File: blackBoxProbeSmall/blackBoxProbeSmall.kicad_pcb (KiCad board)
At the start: 4 copper layers, 44 x 44 mm, 84 parts, among them J1 USB-ID, J2 JTAG_2X05, J3 JTAG_2X05, J4 Conn_01x04, Q1 Q_NMOS_DUAL, Q2 Q_PMOS_DUAL, U1 MCP1702-MB, U2 USBLC6-2, U3 STM32F103CBT, U4 74X2T45, U5 74X2T45, U6 74X2T45, U7 74X2T45, Y1 8.000MHz

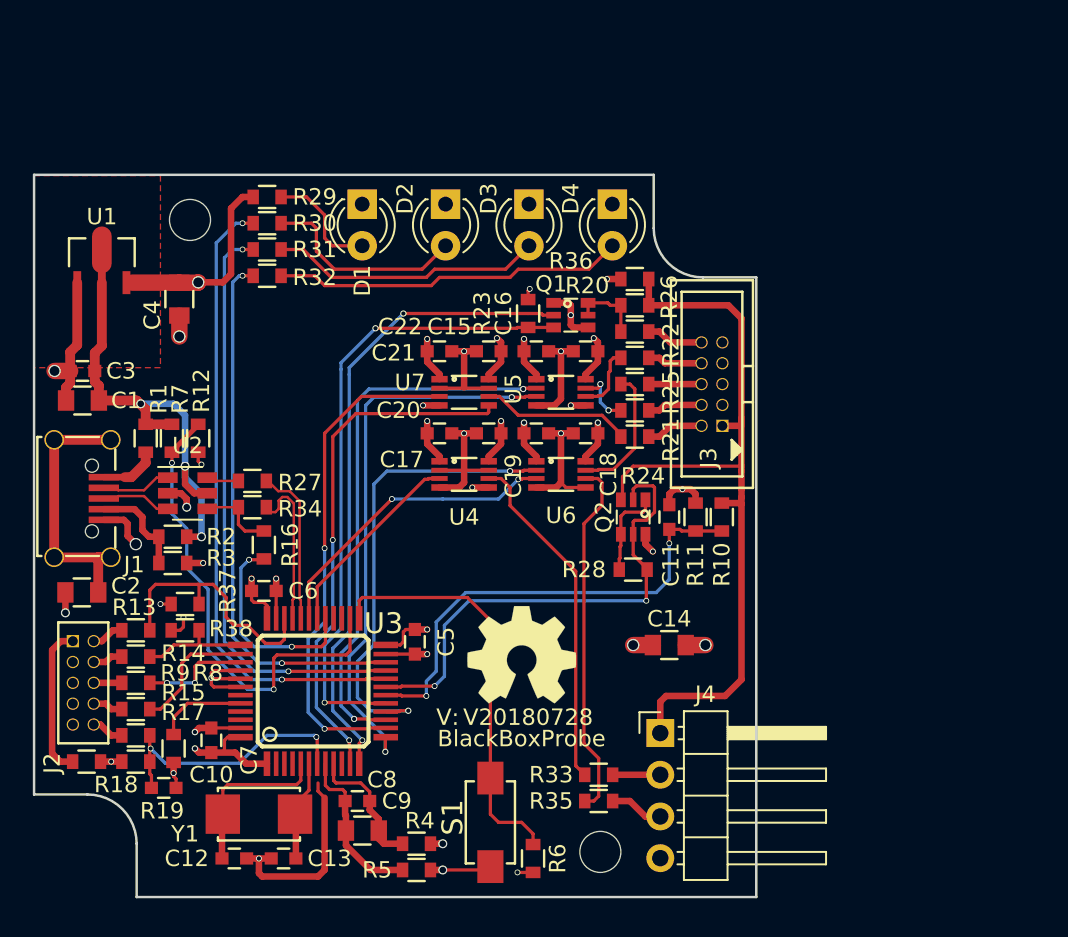
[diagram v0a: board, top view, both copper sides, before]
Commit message: replaced all R's C's and inserted new box outline
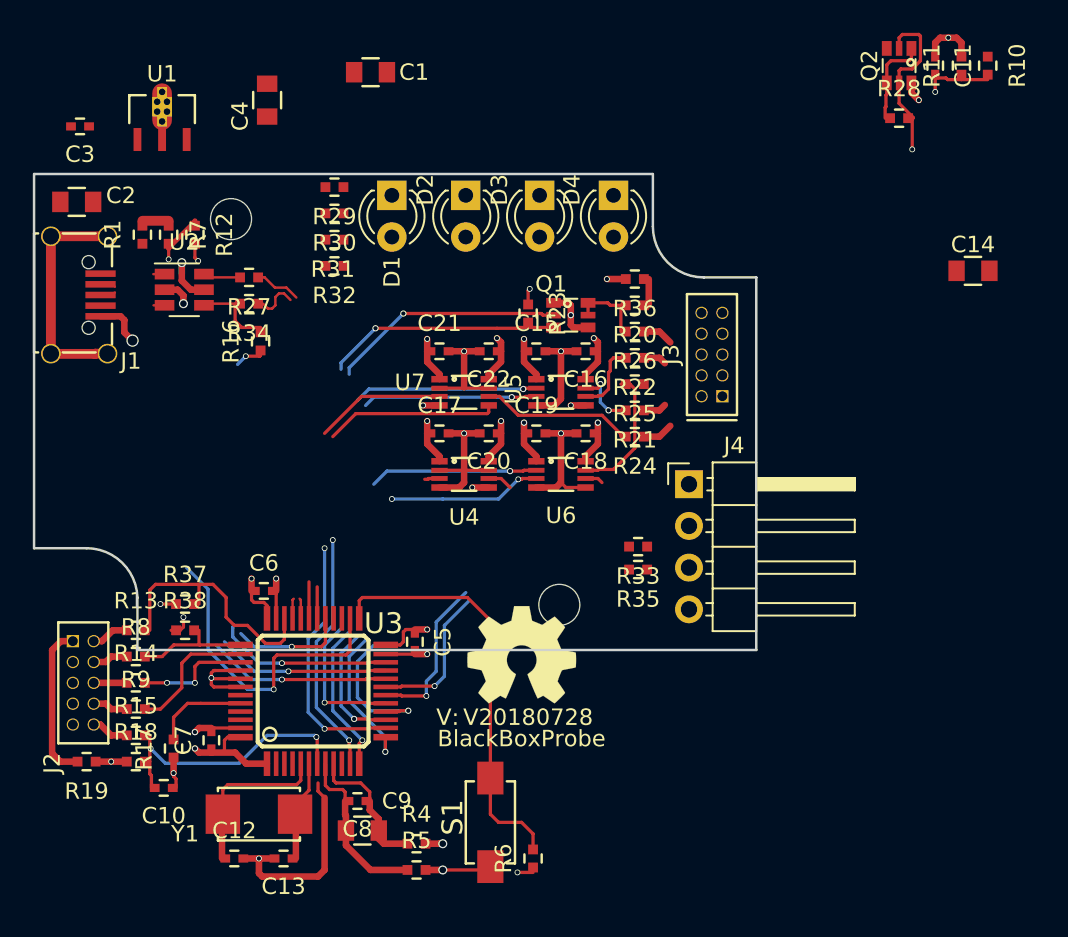
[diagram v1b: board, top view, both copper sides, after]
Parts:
- removed R2, R3: R, SquantorRcl:R_0603_hand
- C10, C11, C12, C13, C15, C16, C17, C18, C19, C20, C21, C22, C3, C5, C6, C7, C8: footprint SquantorRcl:C_0603 -> SquantorRcl:C_0402
- J3: footprint SquantorConnectors:Header-Shr-0127-2X05-H006 -> SquantorConnectors:Header-0127-2X05-H006
- R1, R10, R11, R12, R13, R14, R15, R16, R17, R18, R19, R20, R21, R22, R23, R24, R25, R26, R27, R28, R29, R30, R31, R32, R33, R34, R35, R36, R37, R38, R4, R5, R6, R7, R8, R9: footprint SquantorRcl:R_0603_hand -> SquantorRcl:R_0402_hand
- U1: footprint SquantorMicrochip:MB-(SOT-89) -> SquantorIC:SOT89-ViaTab-Microchip-MB
- moved H2 43.3 mm to (48.4, 235.8)
- moved C11 31.9 mm to (69.2, 144.6)
- moved Q2 31.9 mm to (67.0, 144.6)
- moved R10 31.9 mm to (72.4, 144.6)
- moved R28 31.9 mm to (67.0, 147.8)
- moved R11 31.9 mm to (70.8, 144.6)
- moved C14 29.4 mm to (71.5, 157.1)
- moved C1 26.6 mm to (34.8, 145.0)
- moved C2 23.8 mm to (16.9, 152.9)
- moved J4 15.3 mm to (54.2, 170.1)
- moved C3 14.9 mm to (17.1, 148.3)
- moved R35 14.3 mm to (51.1, 175.3)
- moved R33 14.1 mm to (51.1, 173.9)
- moved C4 13.3 mm to (28.5, 146.7)
- moved J1 12.4 mm to (17.1, 158.6)
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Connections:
- J1 pad 4: Net-(J1-Pad4) -> (no net)
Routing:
- net /PROBE_VDD: track 48.4 -> 1.60 mm
- net /LED0: track 38.5 -> 11.2 mm, vias 2 -> 1
- net /LED1: track 35.9 -> 10.6 mm, vias 2 -> 1
- net +5V: track 29.9 -> 5.13 mm, vias 3 -> 1
- net /LED2: track 33.1 -> 10.7 mm, vias 2 -> 1
- net Net-(D4-Pad2): track 21.4 -> 0.00 mm
- net /PROBE_E_RX: track 22.0 -> 1.10 mm
- net /PROBE_E_TX: track 20.9 -> 1.53 mm
- net Net-(D3-Pad2): track 16.6 -> 0.00 mm
- net /PROBE_I_RST_SEN: track 38.7 -> 22.9 mm
- net /PROBE_I_RST: track 39.2 -> 23.5 mm
- net /TARGET_PWR_SENSE: track 28.8 -> 13.9 mm
- net /PROBE_I_TCK: track 33.3 -> 18.9 mm
- net /PROBE_I_TDI: track 34.0 -> 19.7 mm
- net +3V3: track 52.2 -> 38.8 mm, vias 18 -> 16
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- removed copper zone on F.Cu, net +5V
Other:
- board size 44 x 44 mm -> 44 x 29 mm
